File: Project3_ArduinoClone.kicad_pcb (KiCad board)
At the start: 2 copper layers, 0 parts

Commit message: Import netlist and create netclasses
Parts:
- added BT1: Battery 3V, Connector_PinHeader_2.54mm:PinHeader_1x02_P2.54mm_Vertical, F.Cu at (87.1, 108.6)
- added C1: 22pF, Capacitor_SMD:C_0805_2012Metric_Pad1.15x1.40mm_HandSolder, F.Cu at (167.6, 116.2)
- added C2: 22pF, Capacitor_SMD:C_0805_2012Metric_Pad1.15x1.40mm_HandSolder, F.Cu at (162.1, 121.6)
- added C3: 10uF, Capacitor_SMD:C_0805_2012Metric_Pad1.15x1.40mm_HandSolder, F.Cu at (153.4, 124.6)
- added D1: LED, LED_SMD:LED_0805_2012Metric_Pad1.15x1.40mm_HandSolder, F.Cu at (157.4, 121.6)
- added J1: Serial, Connector_PinSocket_2.54mm:PinSocket_1x04_P2.54mm_Vertical, F.Cu at (80.6, 89.7)
- added J2: Digital pins, Connector_PinSocket_2.54mm:PinSocket_1x09_P2.54mm_Vertical, F.Cu at (76.0, 89.7)
- added J3: ICSP, Connector_PinSocket_2.54mm:PinSocket_2x03_P2.54mm_Vertical, F.Cu at (92.3, 89.7)
- added J4: I2C, Connector_PinSocket_2.54mm:PinSocket_1x04_P2.54mm_Vertical, F.Cu at (85.2, 89.7)
- added R1: 330Ohm, Resistor_SMD:R_0805_2012Metric_Pad1.15x1.40mm_HandSolder, F.Cu at (172.7, 109.0)
- added R2: 10kOhm, Resistor_SMD:R_0805_2012Metric_Pad1.15x1.40mm_HandSolder, F.Cu at (158.2, 124.6)
- added U1: 24LC1025, Package_SO:SOIJ-8_5.3x5.3mm_P1.27mm, F.Cu at (149.7, 118.7)
- added U2: 24LC1025, Package_SO:SOIJ-8_5.3x5.3mm_P1.27mm, F.Cu at (160.4, 111.0)
- added U3: DS1337_v1, Package_SO:SO-8_5.3x6.2mm_P1.27mm, F.Cu at (149.8, 111.4)
- added U4: ATMEGA328P-AU, digikey-footprints:TQFP-32_7x7mm, F.Cu at (159.6, 98.4)
- added Y1: Crystal 32 MHz, Crystal:Crystal_SMD_MicroCrystal_CC7V-T1A-2Pin_3.2x1.5mm_HandSoldering, F.Cu at (147.7, 123.9)
- added Y2: Crystal 16 MHz, Crystal:Crystal_SMD_5032-2Pin_5.0x3.2mm_HandSoldering, F.Cu at (160.1, 117.7)
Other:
- net class Power added: clearance 0.2, trace_width 0.3, via_dia 1, via_drill 0.6

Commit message: First version of the placement
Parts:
- moved U4 79.3 mm to (90.6, 137.3)
- moved C1 75.2 mm to (93.6, 129.5)
- moved R2 74.1 mm to (84.1, 123.2)
- moved Y2 74.1 mm to (86.7, 127.8)
- moved R1 70.1 mm to (109.5, 139.2)
- moved C2 68.8 mm to (93.5, 126.2)
- moved U2 64.6 mm to (101.3, 137.2)
- moved J2 56.3 mm to (88.4, 144.7), turned to 90 degrees
- moved U1 49.3 mm to (101.3, 128.5)
- moved J3 47.1 mm to (82.0, 135.6)
- moved D1 46.2 mm to (114.7, 139.2)
- moved C3 45.8 mm to (108.8, 135.2)
- moved U3 40.8 mm to (112.6, 128.3)
- moved J1 39.9 mm to (104.1, 121.9), turned to 90 degrees
- moved Y1 34.9 mm to (114.7, 135.2)
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
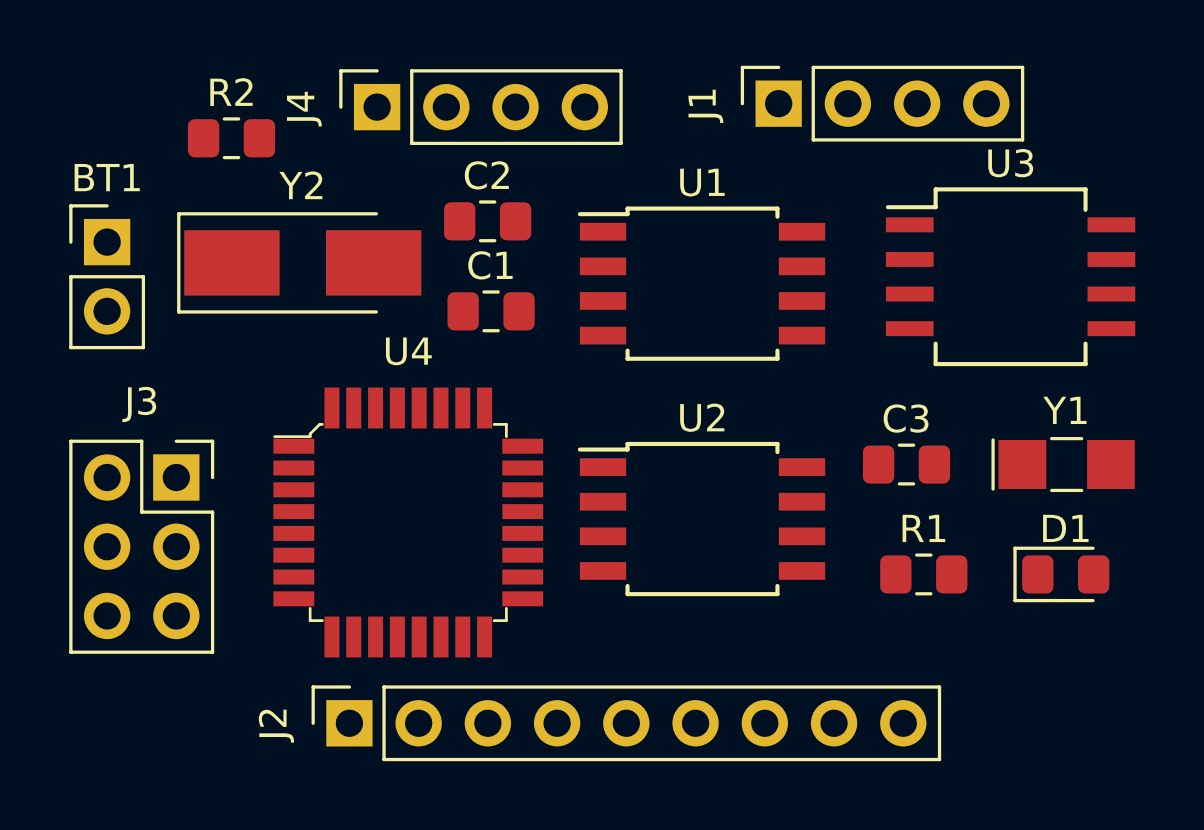
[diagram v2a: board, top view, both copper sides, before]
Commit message: Improve placement, create outline
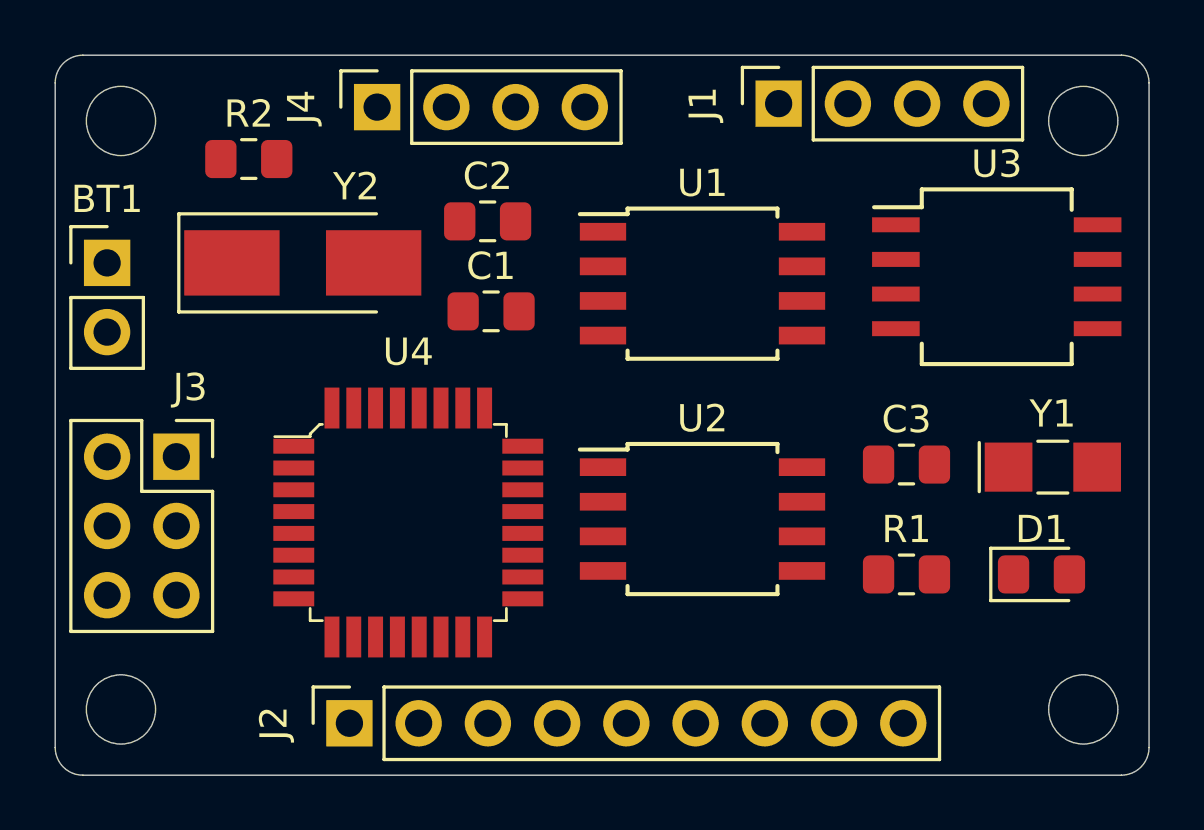
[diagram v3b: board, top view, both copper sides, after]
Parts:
- moved R2 0.99 mm to (84.7, 124.0)
- moved D1 0.89 mm to (113.8, 139.2)
- moved BT1 0.76 mm to (79.5, 127.8)
- moved J3 0.76 mm to (82.0, 134.9)
- moved R1 0.64 mm to (108.8, 139.2)
- moved Y1 0.52 mm to (114.2, 135.3)
- moved U3 0.51 mm to (112.1, 128.3)
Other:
- board outline added: 40.1 x 26.4 mm
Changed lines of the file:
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@@
   (general
     (thickness 1.6)
-    (drawings 0)
+    (drawings 12)
     (tracks 0)
     (zones 0)
@@
   )
   (module Connector_PinHeader_2.54mm:PinHeader_1x02_P2.54mm_Vertical (layer F.Cu)
-    (at 79.502 127)
+    (at 79.502 127.762)
     (descr "Through hole straight pin header, 1x02, 2.54mm pitch, single row")
     (tags "Through hole pin header THT 1x02 2.54mm single row")
@@
   )
   (module LED_SMD:LED_0805_2012Metric_Pad1.15x1.40mm_HandSolder (layer F.Cu)
-    (at 114.672 139.192)
+    (at 113.783 139.192)
     (descr "LED SMD 0805 (2012 Metric), square (rectangular) end terminal, IPC_7351 nominal, (Body size source: https://docs.google.com/spreadsheets/d/1BsfQQcO9C6DZCsRaXUlFlo91Tg2WpOkGARC1WS5S8t0/edit?usp=sharing), generated with kicad-footprint-generator")
     (tags "LED handsolder")
@@
   )
   (module Connector_PinSocket_2.54mm:PinSocket_2x03_P2.54mm_Vertical (layer F.Cu)
-    (at 82.042 135.636)
+    (at 82.042 134.874)
     (descr "Through hole straight socket strip, 2x03, 2.54mm pitch, double cols (from Kicad 4.0.7), script generated")
     (tags "Through hole socket strip THT 2x03 2.54mm double row")
-    (fp_text reference J3 (at -1.27 -2.77) (layer F.SilkS)
+    (fp_text reference J3 (at 0.508 -2.54) (layer F.SilkS)
       (effects (font (size 1 1) (thickness 0.15)))
     )
@@
   )
   (module Resistor_SMD:R_0805_2012Metric_Pad1.15x1.40mm_HandSolder (layer F.Cu)
-    (at 109.465 139.192)
+    (at 108.83 139.192)
     (descr "Resistor SMD 0805 (2012 Metric), square (rectangular) end terminal, IPC_7351 nominal with elongated pad for handsoldering. (Body size source: https://docs.google.com/spreadsheets/d/1BsfQQcO9C6DZCsRaXUlFlo91Tg2WpOkGARC1WS5S8t0/edit?usp=sharing), generated with kicad-footprint-generator")
     (tags "resistor handsolder")
@@
   )
   (module Resistor_SMD:R_0805_2012Metric_Pad1.15x1.40mm_HandSolder (layer F.Cu)
-    (at 84.065 123.19)
+    (at 84.7 123.952)
     (descr "Resistor SMD 0805 (2012 Metric), square (rectangular) end terminal, IPC_7351 nominal with elongated pad for handsoldering. (Body size source: https://docs.google.com/spreadsheets/d/1BsfQQcO9C6DZCsRaXUlFlo91Tg2WpOkGARC1WS5S8t0/edit?usp=sharing), generated with kicad-footprint-generator")
     (tags "resistor handsolder")
@@
   )
   (module Package_SO:SO-8_5.3x6.2mm_P1.27mm (layer F.Cu)
-    (at 112.649 128.27)
+    (at 112.141 128.27)
     (descr "8-Lead Plastic Small Outline, 5.3x6.2mm Body (http://www.ti.com.cn/cn/lit/ds/symlink/tl7705a.pdf)")
     (tags "SOIC 1.27")
@@
   )
   (module Crystal:Crystal_SMD_MicroCrystal_CC7V-T1A-2Pin_3.2x1.5mm_HandSoldering (layer F.Cu)
-    (at 114.707 135.16)
+    (at 114.199 135.255)
     (descr "SMD Crystal MicroCrystal CC7V-T1A/CM7V-T1A series http://www.microcrystal.com/images/_Product-Documentation/01_TF_ceramic_Packages/01_Datasheet/CC1V-T1A.pdf, hand-soldering, 3.2x1.5mm^2 package")
     (tags "SMD SMT crystal hand-soldering")
@@
     (tags "SMD SMT crystal hand-soldering")
     (attr smd)
-    (fp_text reference Y2 (at 0 -2.8) (layer F.SilkS)
+    (fp_text reference Y2 (at 1.965 -2.794) (layer F.SilkS)
       (effects (font (size 1 1) (thickness 0.15)))
     )
@@
       (net 9 /D2))
   )
+  (gr_circle (center 115.316 122.555) (end 115.316 121.285) (layer Edge.Cuts) (width 0.05))
+  (gr_circle (center 115.316 144.145) (end 115.316 142.875) (layer Edge.Cuts) (width 0.05))
+  (gr_circle (center 80.01 144.145) (end 80.01 142.875) (layer Edge.Cuts) (width 0.05))
+  (gr_circle (center 80.01 122.555) (end 80.01 121.285) (layer Edge.Cuts) (width 0.05))
+  (gr_arc (start 116.713 145.542) (end 116.713 146.558) (angle -90) (layer Edge.Cuts) (width 0.05))
+  (gr_arc (start 116.713 121.158) (end 117.729 121.158) (angle -90) (layer Edge.Cuts) (width 0.05))
+  (gr_arc (start 78.613 121.158) (end 78.613 120.142) (angle -90) (layer Edge.Cuts) (width 0.05))
+  (gr_arc (start 78.613 145.542) (end 77.597 145.542) (angle -90) (layer Edge.Cuts) (width 0.05))
+  (gr_line (start 117.729 145.542) (end 117.729 121.158) (layer Edge.Cuts) (width 0.05))
+  (gr_line (start 78.613 146.558) (end 116.713 146.558) (layer Edge.Cuts) (width 0.05))
+  (gr_line (start 77.597 121.158) (end 77.597 145.542) (layer Edge.Cuts) (width 0.05))
+  (gr_line (start 116.713 120.142) (end 78.613 120.142) (layer Edge.Cuts) (width 0.05))
 )
